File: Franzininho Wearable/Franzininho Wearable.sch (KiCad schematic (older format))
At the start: 17 parts, among them U1 ICL7660SCPAZ, U2 LM324N_NOPB, U3 LM324N_NOPB

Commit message: Ajuste no caminho das bibilotecas locais e referencia do segundo ampop
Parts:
- removed U3: LM324N_NOPB, DIP825W47P254L1917H533Q14, symbol LM324N_NOPB:LM324N_NOPB
- added unit 2 of U2
- U2: symbol LM324N_NOPB:LM324N_NOPB -> Franzininho-Wearable-rescue:LM324N_NOPB-LM324N_NOPB
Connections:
- net AMP: now also U2.7
- net at R7.1: now also U2.6
- net at R8.1: now also U2.5
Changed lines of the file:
@@
 	6800 1850 6750 1850
 $Comp
-L LM324N_NOPB:LM324N_NOPB U2
+L Franzininho-Wearable-rescue:LM324N_NOPB-LM324N_NOPB U2
 U 4 1 60F8F90E
 P 7250 5650
@@
 $EndComp
 $Comp
-L LM324N_NOPB:LM324N_NOPB U2
+L Franzininho-Wearable-rescue:LM324N_NOPB-LM324N_NOPB U2
 U 3 1 60F8EE3A
 P 7450 4300
@@
 F 7 "Texas Instruments" H 7250 1950 50  0001 L BNN "MANUFACTURER"
 	1    7250 1950
-	1    0    0    -1
-$EndComp
-$Comp
-L LM324N_NOPB:LM324N_NOPB U3
-U 1 1 60F7B994
-P 8850 2050
-F 0 "U3" H 9050 2250 50  0000 L CNN
-F 1 "LM324N_NOPB" H 9050 2150 50  0000 L CNN
-F 2 "DIP825W47P254L1917H533Q14" H 8850 2050 50  0001 L BNN
-F 3 "" H 8850 2050 50  0001 L BNN
-F 4 "5.08mm" H 8850 2050 50  0001 L BNN "MAXIMUM_PACKAGE_HEIGHT"
-F 5 "IPC-7351B" H 8850 2050 50  0001 L BNN "STANDARD"
-F 6 "D" H 8850 2050 50  0001 L BNN "PARTREV"
-F 7 "Texas Instruments" H 8850 2050 50  0001 L BNN "MANUFACTURER"
-	1    8850 2050
 	1    0    0    -1
 $EndComp
@@
 	1    0    0    -1
 $EndComp
+$Comp
+L LM324N_NOPB:LM324N_NOPB U2
+U 2 1 60F9C21F
+P 8850 2050
+F 0 "U2" H 9000 2300 50  0000 L CNN
+F 1 "LM324N_NOPB" H 9000 2200 50  0000 L CNN
+F 2 "DIP825W47P254L1917H533Q14" H 8850 2050 50  0001 L BNN
+F 3 "" H 8850 2050 50  0001 L BNN
+F 4 "5.08mm" H 8850 2050 50  0001 L BNN "MAXIMUM_PACKAGE_HEIGHT"
+F 5 "IPC-7351B" H 8850 2050 50  0001 L BNN "STANDARD"
+F 6 "D" H 8850 2050 50  0001 L BNN "PARTREV"
+F 7 "Texas Instruments" H 8850 2050 50  0001 L BNN "MANUFACTURER"
+	2    8850 2050
+	1    0    0    -1
+$EndComp

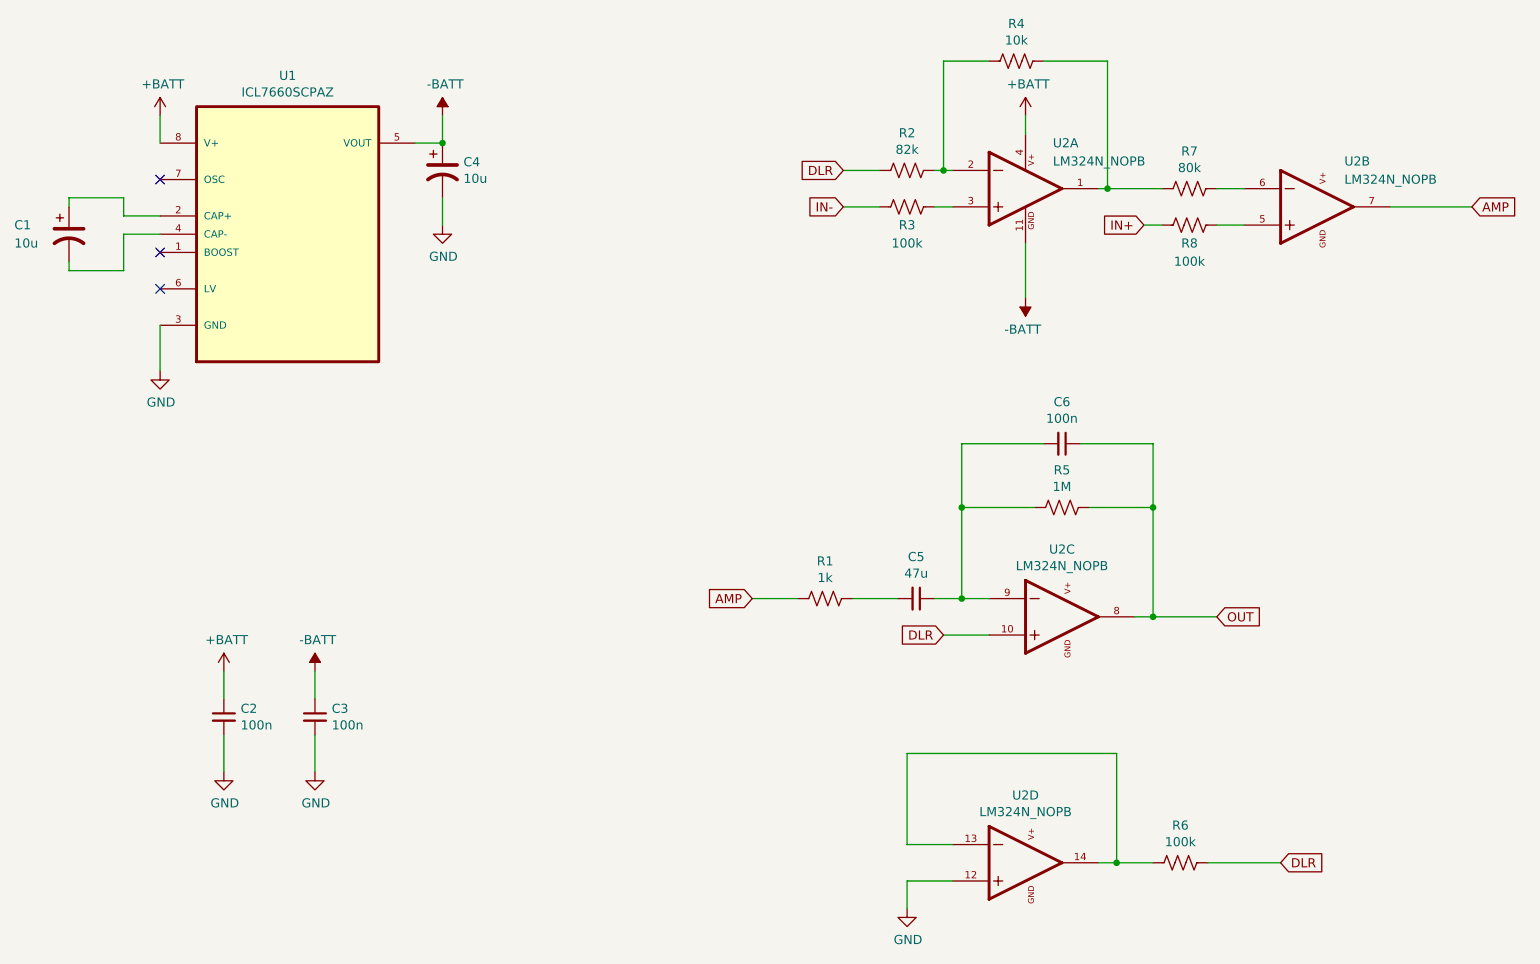
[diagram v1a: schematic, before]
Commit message: - Adicionado .gitignore para .bck e .sch-bck - Alteradas labels globais para locais e hierárquicas - Dividido circuito em folhas
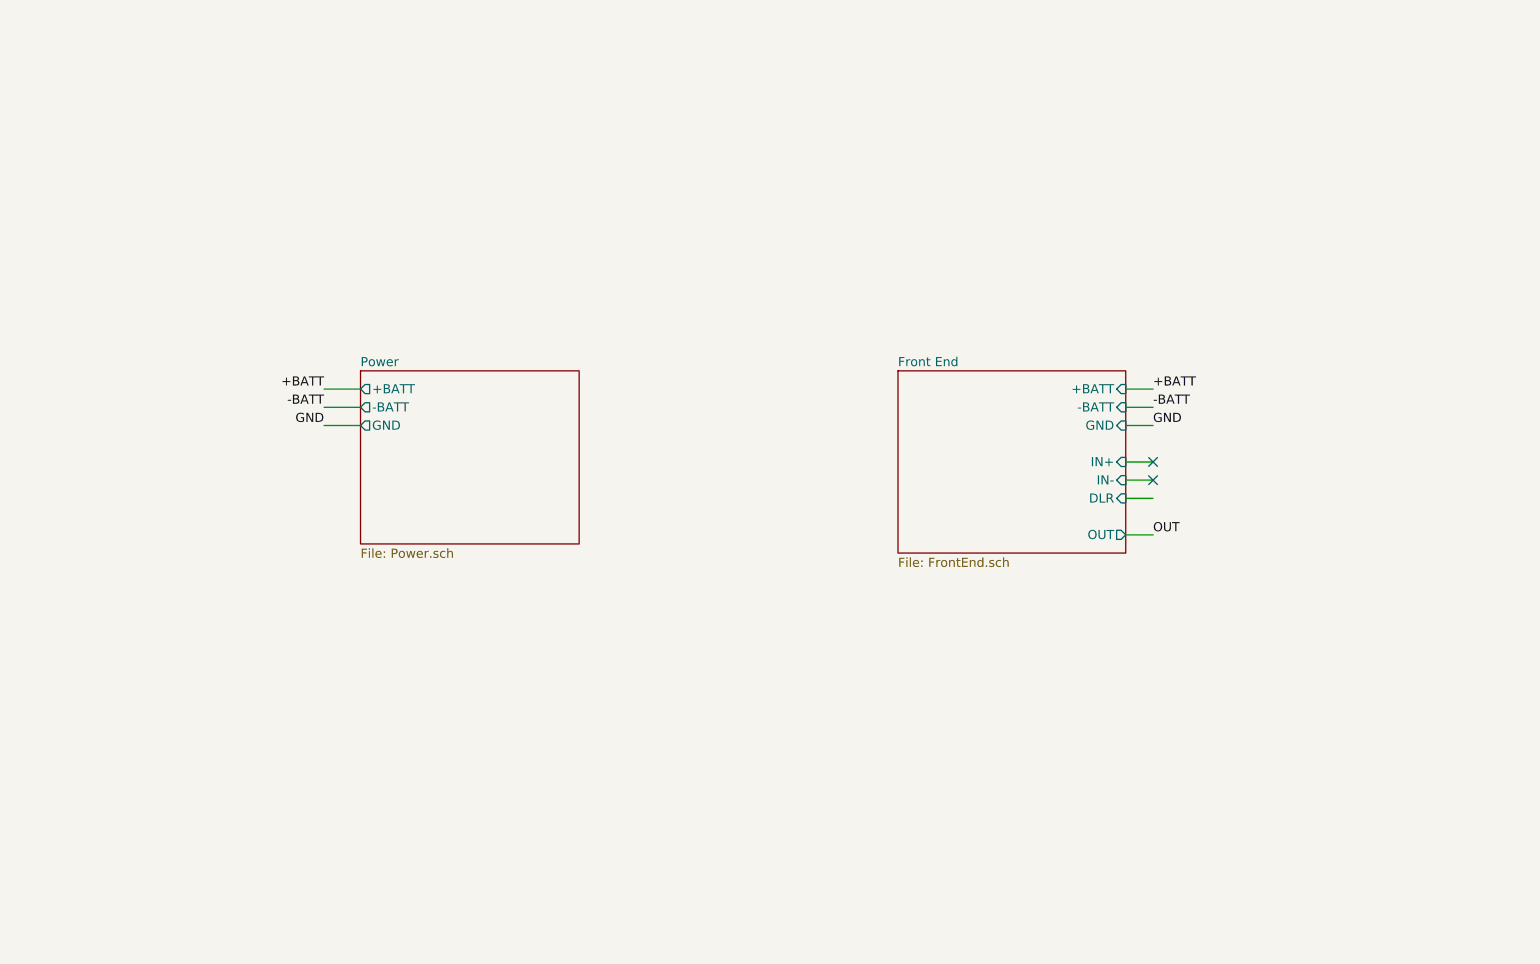
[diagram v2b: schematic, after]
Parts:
- removed C1, C4: 10u, symbol Device:CP1
- removed C2, C3, C6: 100n, symbol Device:C_Small
- removed C5: 47u, symbol Device:C_Small
- removed R1: 1k, symbol Device:R_US
- removed R2: 82k, symbol Device:R_US
- removed R3, R6, R8: 100k, symbol Device:R_US
- removed R4: 10k, symbol Device:R_US
- removed R5: 1M, symbol Device:R_US
- removed R7: 80k, symbol Device:R_US
- removed U1: ICL7660SCPAZ, DIP254P762X533-8, symbol ICL7660SCPAZ:ICL7660SCPAZ
- removed U2: LM324N_NOPB, DIP825W47P254L1917H533Q14, symbol LM324N_NOPB:LM324N_NOPB
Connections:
- net labels removed: AMP, DLR, IN+, IN-
- wire segments 58 -> 10
- no-connect marks 3 -> 2
